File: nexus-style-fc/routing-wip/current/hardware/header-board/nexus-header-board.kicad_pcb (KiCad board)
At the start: 2 copper layers, 22.4 x 11 mm, 12 parts, among them J1 Servo header 3x7, K1 GND strip, K2 VX strip, P1 S1 tab pad, P2 S2 tab pad, P3 S3 tab pad, P4 TAIL tab pad, P5 ESC tab pad, P6 RPM tab pad, P7 SBUS tab pad, T1 GND tab pad, T2 VX tab pad

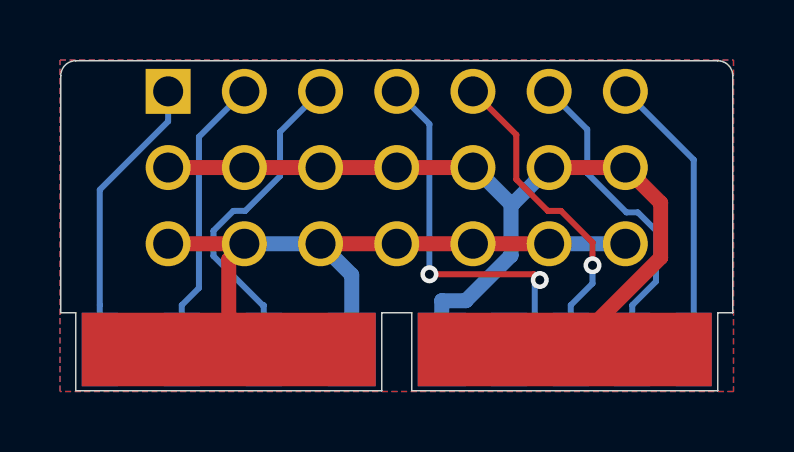
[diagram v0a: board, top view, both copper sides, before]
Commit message: Nexus WIP: integrate zero-error header interface and restore signal returns
Keep current candidate atomic with matching main/child source, native evidence and WIP exports. Physical assembly, manufacturing process and electrical qualification remain open. No unrelated project changes.
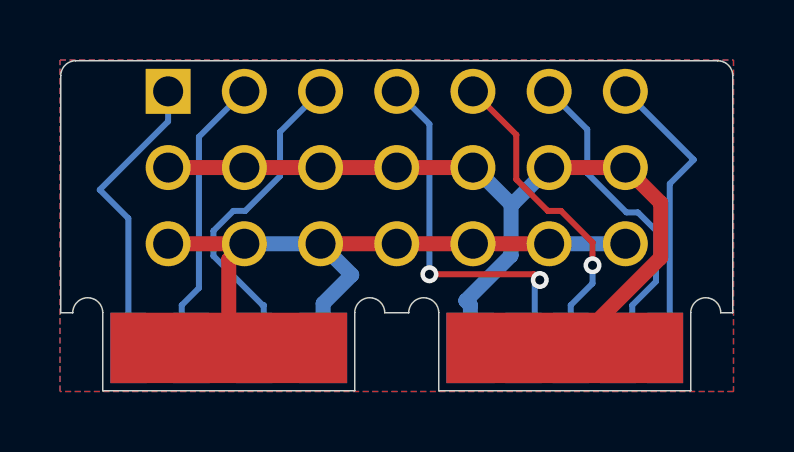
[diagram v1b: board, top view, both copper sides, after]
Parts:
- K1, K2: footprint NexusFC:ChildBoard_TabStrip_W9.8 -> NexusFC:ChildBoard_TabStrip_W7.892
- moved P1 0.95 mm to (102.3, 108.4)
- moved T1 0.95 mm to (108.7, 108.4)
- moved P7 0.95 mm to (120.1, 108.4)
- moved T2 0.95 mm to (113.7, 108.4)
- moved P4 0.48 mm to (115.4, 108.4)
- moved P6 0.48 mm to (118.6, 108.4)
- moved P2 0.32 mm to (104.4, 108.4)
- moved P3 0.32 mm to (106.4, 108.4)
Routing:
- net VX: track 30.5 -> 29.7 mm
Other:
- outline, holes or cut-outs redrawn
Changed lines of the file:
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@@
 	(footprint "NexusFC:ChildBoard_TabPad_Pwr"
 		(layer "F.Cu")
-		(at 112.7 108.4)
+		(at 113.654 108.4)
 		(descr "Child-board tab pad, 1.6 mm wide, inner face (B.Cu), from 0.0 mm above the main-board surface to the tab end. Origin on the seating line")
 		(property "Reference" "T2"
@@
 		(duplicate_pad_numbers_are_jumpers no)
 		(pad "1" smd rect
-			(at 0 1.225)
-			(size 1.6 2.45)
+			(at 0 1.173)
+			(size 1.6 2.346)
 			(layers "B.Cu" "B.Mask")
 			(net "VX")
@@
 		(embedded_fonts no)
 	)
-	(footprint "NexusFC:ChildBoard_TabStrip_W9.8"
+	(footprint "NexusFC:ChildBoard_TabStrip_W7.892"
 		(layer "F.Cu")
 		(at 116.8 108.4)
-		(descr "Child-board outer-face strip, 9.80 mm wide (F.Cu), from 0.0 mm above the main-board surface (below the header body) to the tab end. Origin on the seating line, tab centre")
+		(descr "UNFINISHED root-aware child outer-face strip, 7.892 mm wide, 2.346 mm tall")
 		(property "Reference" "K2"
 			(at 0 -1.6 0)
@@
 		(duplicate_pad_numbers_are_jumpers no)
 		(pad "1" smd rect
-			(at 0 1.225)
-			(size 9.8 2.45)
+			(at 0 1.173)
+			(size 7.892 2.346)
 			(layers "F.Cu" "F.Mask")
 			(net "VX")
@@
 	(footprint "NexusFC:ChildBoard_TabPad_Sig"
 		(layer "F.Cu")
-		(at 121.1 108.4)
+		(at 120.146 108.4)
 		(descr "Child-board tab pad, 1.2 mm wide, inner face (B.Cu), from 0.0 mm above the main-board surface to the tab end. Origin on the seating line")
 		(property "Reference" "P7"
@@
 		(duplicate_pad_numbers_are_jumpers no)
 		(pad "1" smd rect
-			(at 0 1.225)
-			(size 1.2 2.45)
+			(at 0 1.173)
+			(size 1.2 2.346)
 			(layers "B.Cu" "B.Mask")
 			(net "SBUS")
@@
 	(footprint "NexusFC:ChildBoard_TabPad_Sig"
 		(layer "F.Cu")
-		(at 101.3 108.4)
+		(at 102.254 108.4)
 		(descr "Child-board tab pad, 1.2 mm wide, inner face (B.Cu), from 0.0 mm above the main-board surface to the tab end. Origin on the seating line")
 		(property "Reference" "P1"
@@
 		(duplicate_pad_numbers_are_jumpers no)
 		(pad "1" smd rect
-			(at 0 1.225)
-			(size 1.2 2.45)
+			(at 0 1.173)
+			(size 1.2 2.346)
 			(layers "B.Cu" "B.Mask")
 			(net "S1")
@@
 	(footprint "NexusFC:ChildBoard_TabPad_Sig"
 		(layer "F.Cu")
-		(at 114.95 108.4)
+		(at 115.427 108.4)
 		(descr "Child-board tab pad, 1.2 mm wide, inner face (B.Cu), from 0.0 mm above the main-board surface to the tab end. Origin on the seating line")
 		(property "Reference" "P4"
@@
 		(duplicate_pad_numbers_are_jumpers no)
 		(pad "1" smd rect
-			(at 0 1.225)
-			(size 1.2 2.45)
+			(at 0 1.173)
+			(size 1.2 2.346)
 			(layers "B.Cu" "B.Mask")
 			(net "TAIL")
@@
 		(embedded_fonts no)
 	)
-	(footprint "NexusFC:ChildBoard_TabStrip_W9.8"
+	(footprint "NexusFC:ChildBoard_TabStrip_W7.892"
 		(layer "F.Cu")
 		(at 105.6 108.4)
-		(descr "Child-board outer-face strip, 9.80 mm wide (F.Cu), from 0.0 mm above the main-board surface (below the header body) to the tab end. Origin on the seating line, tab centre")
+		(descr "UNFINISHED root-aware child outer-face strip, 7.892 mm wide, 2.346 mm tall")
 		(property "Reference" "K1"
 			(at 0 -1.6 0)
@@
 		(duplicate_pad_numbers_are_jumpers no)
 		(pad "1" smd rect
-			(at 0 1.225)
-			(size 9.8 2.45)
+			(at 0 1.173)
+			(size 7.892 2.346)
 			(layers "F.Cu" "F.Mask")
 			(net "GND")
@@
 	(footprint "NexusFC:ChildBoard_TabPad_Sig"
 		(layer "F.Cu")
-		(at 104.0333 108.4)
+		(at 104.351333 108.4)
 		(descr "Child-board tab pad, 1.2 mm wide, inner face (B.Cu), from 0.0 mm above the main-board surface to the tab end. Origin on the seating line")
 		(property "Reference" "P2"
@@
 		(duplicate_pad_numbers_are_jumpers no)
 		(pad "1" smd rect
-			(at 0 1.225)
-			(size 1.2 2.45)
+			(at 0 1.173)
+			(size 1.2 2.346)
 			(layers "B.Cu" "B.Mask")
 			(net "S2")
@@
 		(duplicate_pad_numbers_are_jumpers no)
 		(pad "1" smd rect
-			(at 0 1.225)
-			(size 1.2 2.45)
+			(at 0 1.173)
+			(size 1.2 2.346)
 			(layers "B.Cu" "B.Mask")
 			(net "ESC")
@@
 	(footprint "NexusFC:ChildBoard_TabPad_Sig"
 		(layer "F.Cu")
-		(at 106.7667 108.4)
+		(at 106.448667 108.4)
 		(descr "Child-board tab pad, 1.2 mm wide, inner face (B.Cu), from 0.0 mm above the main-board surface to the tab end. Origin on the seating line")
 		(property "Reference" "P3"
@@
 		(duplicate_pad_numbers_are_jumpers no)
 		(pad "1" smd rect
-			(at 0 1.225)
-			(size 1.2 2.45)
+			(at 0 1.173)
+			(size 1.2 2.346)
 			(layers "B.Cu" "B.Mask")
 			(net "S3")
@@
 	(footprint "NexusFC:ChildBoard_TabPad_Sig"
 		(layer "F.Cu")
-		(at 119.05 108.4)
+		(at 118.573 108.4)
 		(descr "Child-board tab pad, 1.2 mm wide, inner face (B.Cu), from 0.0 mm above the main-board surface to the tab end. Origin on the seating line")
 		(property "Reference" "P6"
@@
 		(duplicate_pad_numbers_are_jumpers no)
 		(pad "1" smd rect
-			(at 0 1.225)
-			(size 1.2 2.45)
+			(at 0 1.173)
+			(size 1.2 2.346)
 			(layers "B.Cu" "B.Mask")
 			(net "RPM")
@@
 	(footprint "NexusFC:ChildBoard_TabPad_Pwr"
 		(layer "F.Cu")
-		(at 109.7 108.4)
+		(at 108.746 108.4)
 		(descr "Child-board tab pad, 1.6 mm wide, inner face (B.Cu), from 0.0 mm above the main-board surface to the tab end. Origin on the seating line")
 		(property "Reference" "T1"
@@
 		(duplicate_pad_numbers_are_jumpers no)
 		(pad "1" smd rect
-			(at 0 1.225)
-			(size 1.6 2.45)
+			(at 0 1.173)
+			(size 1.6 2.346)
 			(layers "B.Cu" "B.Mask")
 			(net "GND")
@@
 	(gr_line
 		(start 100 108.4)
-		(end 100.5 108.4)
-		(stroke
-			(width 0.05)
-			(type default)
+		(end 100.4 108.4)
+		(stroke
+			(width 0.05)
+			(type solid)
+		)
+		(layer "Edge.Cuts")
+	)
+	(gr_arc
+		(start 100.4 108.4)
+		(mid 100.9 107.9)
+		(end 101.4 108.4)
+		(stroke
+			(width 0.05)
+			(type solid)
 		)
 		(layer "Edge.Cuts")
@@
 	)
 	(gr_line
-		(start 100.5 108.4)
-		(end 100.5 111)
-		(stroke
-			(width 0.05)
-			(type default)
+		(start 101.4 108.4)
+		(end 101.4 111)
+		(stroke
+			(width 0.05)
+			(type solid)
 		)
 		(layer "Edge.Cuts")
 	)
 	(gr_line
-		(start 100.5 111)
-		(end 110.7 111)
-		(stroke
-			(width 0.05)
-			(type default)
+		(start 101.4 111)
+		(end 109.8 111)
+		(stroke
+			(width 0.05)
+			(type solid)
+		)
+		(layer "Edge.Cuts")
+	)
+	(gr_arc
+		(start 109.8 108.4)
+		(mid 110.3 107.9)
+		(end 110.8 108.4)
+		(stroke
+			(width 0.05)
+			(type solid)
 		)
 		(layer "Edge.Cuts")
 	)
 	(gr_line
-		(start 110.7 108.4)
-		(end 111.7 108.4)
-		(stroke
-			(width 0.05)
-			(type default)
+		(start 109.8 111)
+		(end 109.8 108.4)
+		(stroke
+			(width 0.05)
+			(type solid)
 		)
 		(layer "Edge.Cuts")
 	)
 	(gr_line
-		(start 110.7 111)
-		(end 110.7 108.4)
-		(stroke
-			(width 0.05)
-			(type default)
+		(start 110.8 108.4)
+		(end 111.6 108.4)
+		(stroke
+			(width 0.05)
+			(type solid)
+		)
+		(layer "Edge.Cuts")
+	)
+	(gr_arc
+		(start 111.6 108.4)
+		(mid 112.1 107.9)
+		(end 112.6 108.4)
+		(stroke
+			(width 0.05)
+			(type solid)
 		)
 		(layer "Edge.Cuts")
 	)
 	(gr_line
-		(start 111.7 108.4)
-		(end 111.7 111)
-		(stroke
-			(width 0.05)
-			(type default)
+		(start 112.6 108.4)
+		(end 112.6 111)
+		(stroke
+			(width 0.05)
+			(type solid)
 		)
 		(layer "Edge.Cuts")
 	)
 	(gr_line
-		(start 111.7 111)
-		(end 121.9 111)
-		(stroke
-			(width 0.05)
-			(type default)
+		(start 112.6 111)
+		(end 121 111)
+		(stroke
+			(width 0.05)
+			(type solid)
+		)
+		(layer "Edge.Cuts")
+	)
+	(gr_arc
+		(start 121 108.4)
+		(mid 121.5 107.9)
+		(end 122 108.4)
+		(stroke
+			(width 0.05)
+			(type solid)
+		)
+		(layer "Edge.Cuts")
+	)
+	(gr_line
+		(start 121 111)
+		(end 121 108.4)
+		(stroke
+			(width 0.05)
+			(type solid)
 		)
 		(layer "Edge.Cuts")
@@
 	)
 	(gr_line
-		(start 121.9 108.4)
+		(start 122 108.4)
 		(end 122.4 108.4)
 		(stroke
 			(width 0.05)
-			(type default)
-		)
-		(layer "Edge.Cuts")
-	)
-	(gr_line
-		(start 121.9 111)
-		(end 121.9 108.4)
-		(stroke
-			(width 0.05)
-			(type default)
+			(type solid)
 		)
 		(layer "Edge.Cuts")
@@
 	(segment
 		(start 113.5022 107.9983)
-		(end 112.7 107.9983)
+		(end 113.654 108.1501)
 		(width 0.5)
 		(layer "B.Cu")
@@
 	)
 	(segment
-		(start 112.7 109.625)
-		(end 112.7 107.9983)
-		(width 0.5)
-		(layer "B.Cu")
-		(net "VX")
+		(start 113.654 108.1501)
+		(end 113.654 109.573)
+		(width 0.5)
+		(layer "B.Cu")
+		(net "VX")
+	)
+	(segment
+		(start 120.3 104.1)
+		(end 120.3 109.573)
+		(width 0.2)
+		(layer "B.Cu")
+		(net "SBUS")
 	)
 	(segment
 		(start 121.1 103.3)
-		(end 121.1 109.625)
+		(end 120.3 104.1)
+		(width 0.2)
+		(layer "B.Cu")
+		(net "SBUS")
+	)
+	(segment
+		(start 120.3 109.573)
+		(end 120.146 109.573)
 		(width 0.2)
 		(layer "B.Cu")
@@
 	(segment
 		(start 101.3 104.3017)
-		(end 101.3 108.1483)
+		(end 102.254 105.2557)
 		(width 0.2)
 		(layer "B.Cu")
@@
 	)
 	(segment
-		(start 101.3 109.625)
-		(end 101.3 108.1483)
+		(start 102.254 105.2557)
+		(end 102.254 109.573)
 		(width 0.2)
 		(layer "B.Cu")
@@
 	)
 	(segment
+		(start 108.746 108.094)
+		(end 108.746 109.573)
+		(width 0.5)
+		(layer "B.Cu")
+		(net "GND")
+	)
+	(segment
 		(start 108.66 106.1)
 		(end 109.7 107.14)
@@
 	(segment
 		(start 109.7 107.14)
-		(end 109.7 109.625)
-		(width 0.5)
-		(layer "B.Cu")
+		(end 108.746 108.094)
+		(width 0.5)
+		(layer "B.Cu")
